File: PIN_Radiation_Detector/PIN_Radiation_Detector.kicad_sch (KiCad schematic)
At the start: 21 parts, among them J1 Conn_01x03, Q1 MMBF4392LT1G, U1 LM358DR

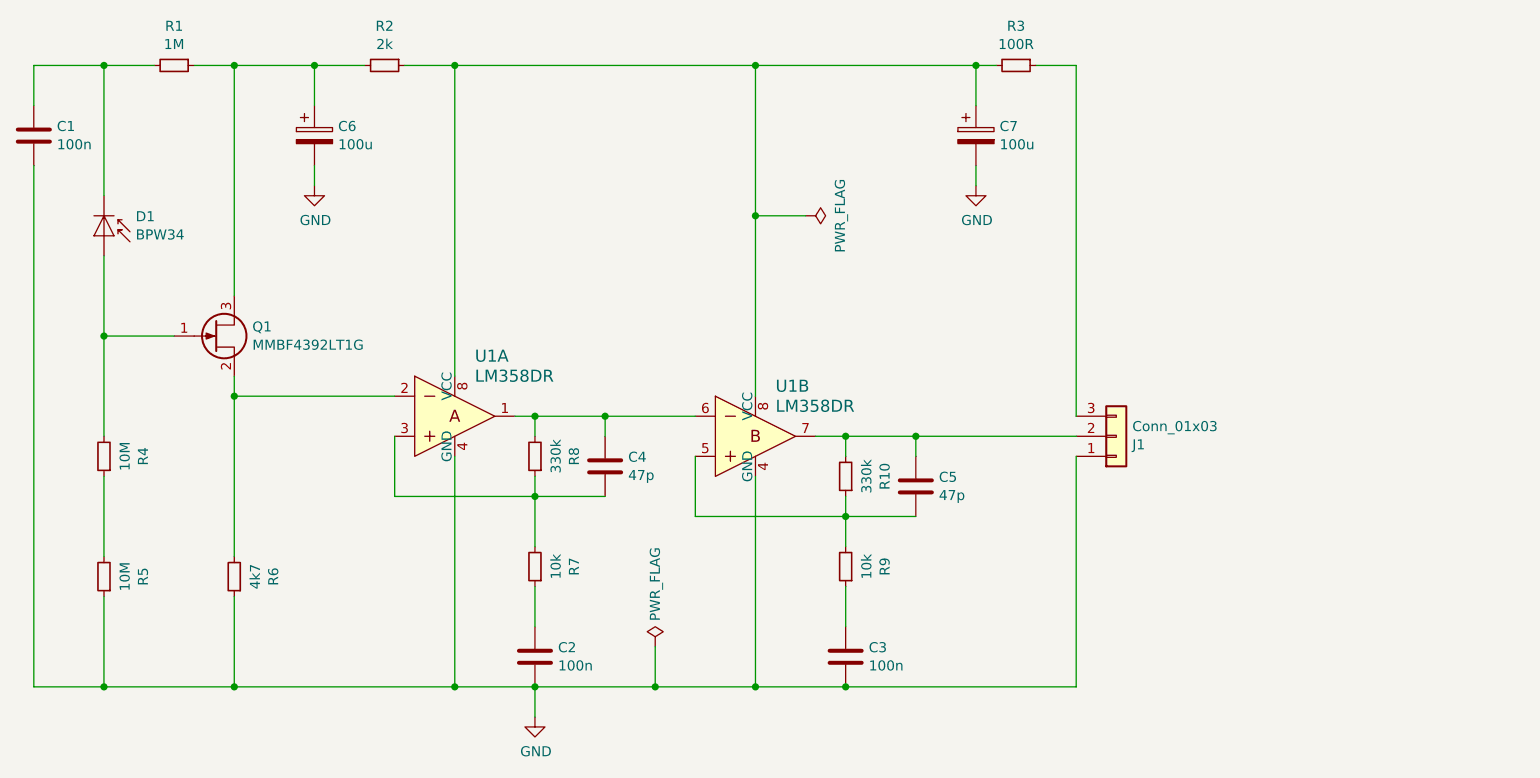
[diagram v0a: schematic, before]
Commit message: Add PDF schematic plot and minor text notes
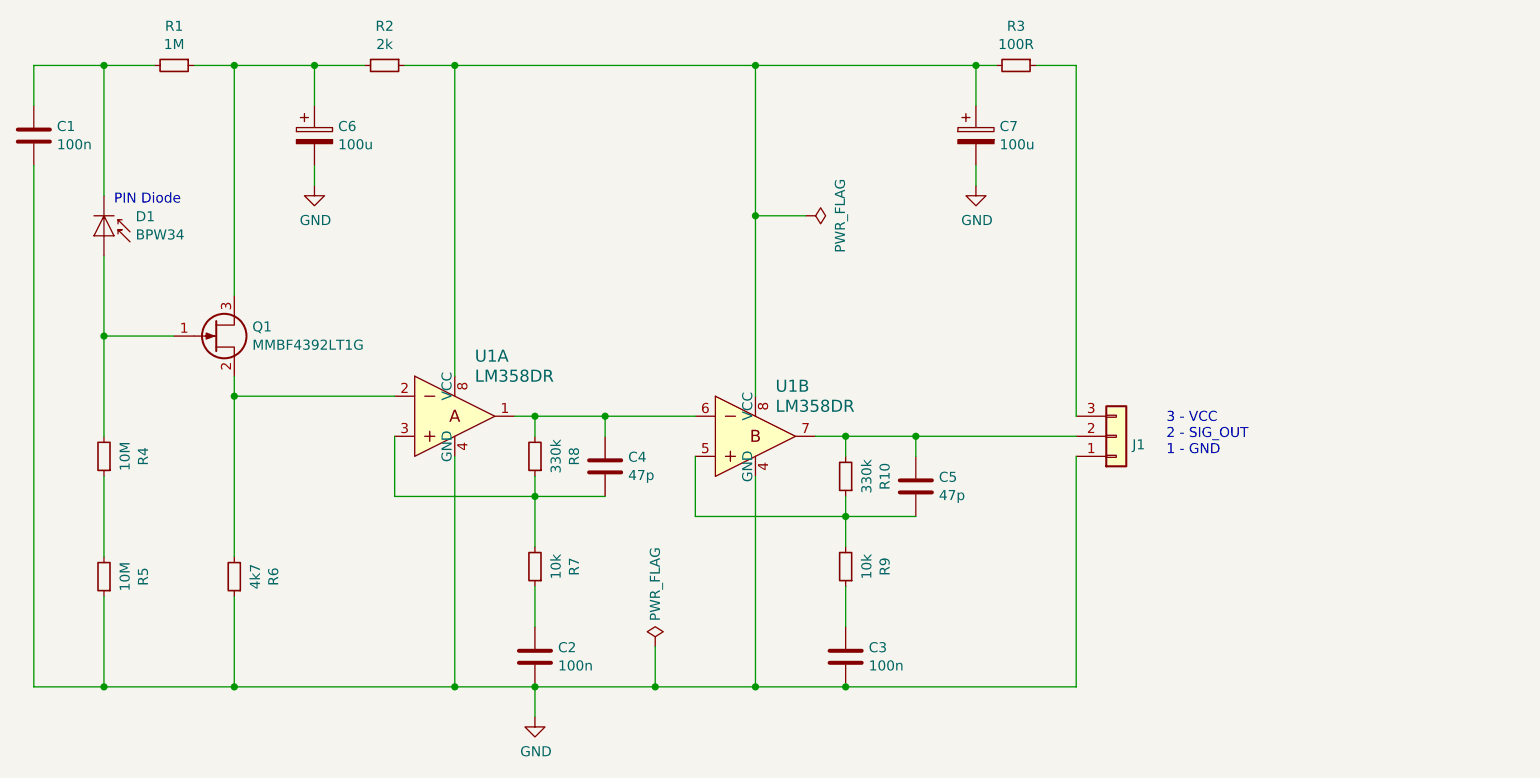
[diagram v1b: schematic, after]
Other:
- note added: "3 - VCC 2 - SIG_OUT 1 - GND"
- note added: "PIN Diode"
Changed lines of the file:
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@@
 (kicad_sch (version 20230121) (generator eeschema)
-  (paper "A4")
+  (paper "USLetter")
   (title_block
     (title "PIN Diode Radiation Detector Breakout")
@@
     (stroke (width 0) (type default))
   )
+  (text "3 - VCC\n2 - SIG_OUT\n1 - GND" (at 219.71 92.71 0)
+    (effects (font (size 1.27 1.27)) (justify left bottom))
+  )
+  (text "PIN Diode" (at 86.36 60.96 0)
+    (effects (font (size 1.27 1.27)) (justify left bottom))
+  )
   (symbol (lib_id "Sensor_Optical:BPW34") (at 85.09 64.77 270) (unit 1)
     (in_bom yes) (on_board yes) (dnp no)
@@
     )
     (property "Value" "Conn_01x03" (at 215.392 88.9254 0)
-      (effects (font (size 1.27 1.27)) (justify left))
+      (effects (font (size 1.27 1.27)) (justify left) hide)
     )
     (property "Footprint" "Pin_Headers:Pin_Header_Straight_1x03_Pitch2.54mm" (at 213.36 90.17 0)

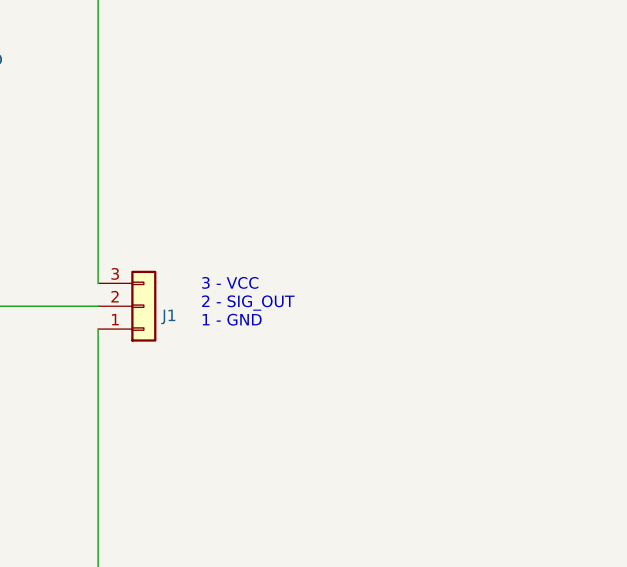
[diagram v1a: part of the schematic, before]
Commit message: Add VCC=5V recommended note
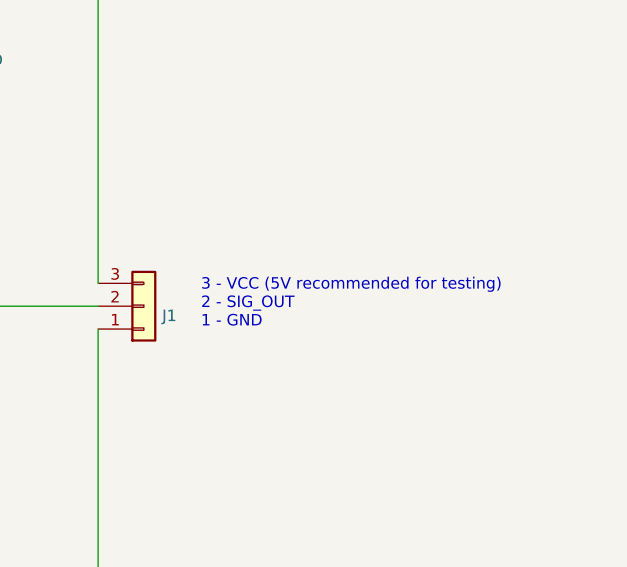
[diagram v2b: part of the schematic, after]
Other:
- note added: "3 - VCC (5V recommended for testing) 2 - SIG_OUT 1 - GND"
- note removed: "3 - VCC 2 - SIG_OUT 1 - GND"
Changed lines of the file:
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@@
     (stroke (width 0) (type default))
   )
-  (text "3 - VCC\n2 - SIG_OUT\n1 - GND" (at 219.71 92.71 0)
+  (text "3 - VCC (5V recommended for testing)\n2 - SIG_OUT\n1 - GND"
+    (at 219.71 92.71 0)
     (effects (font (size 1.27 1.27)) (justify left bottom))
   )

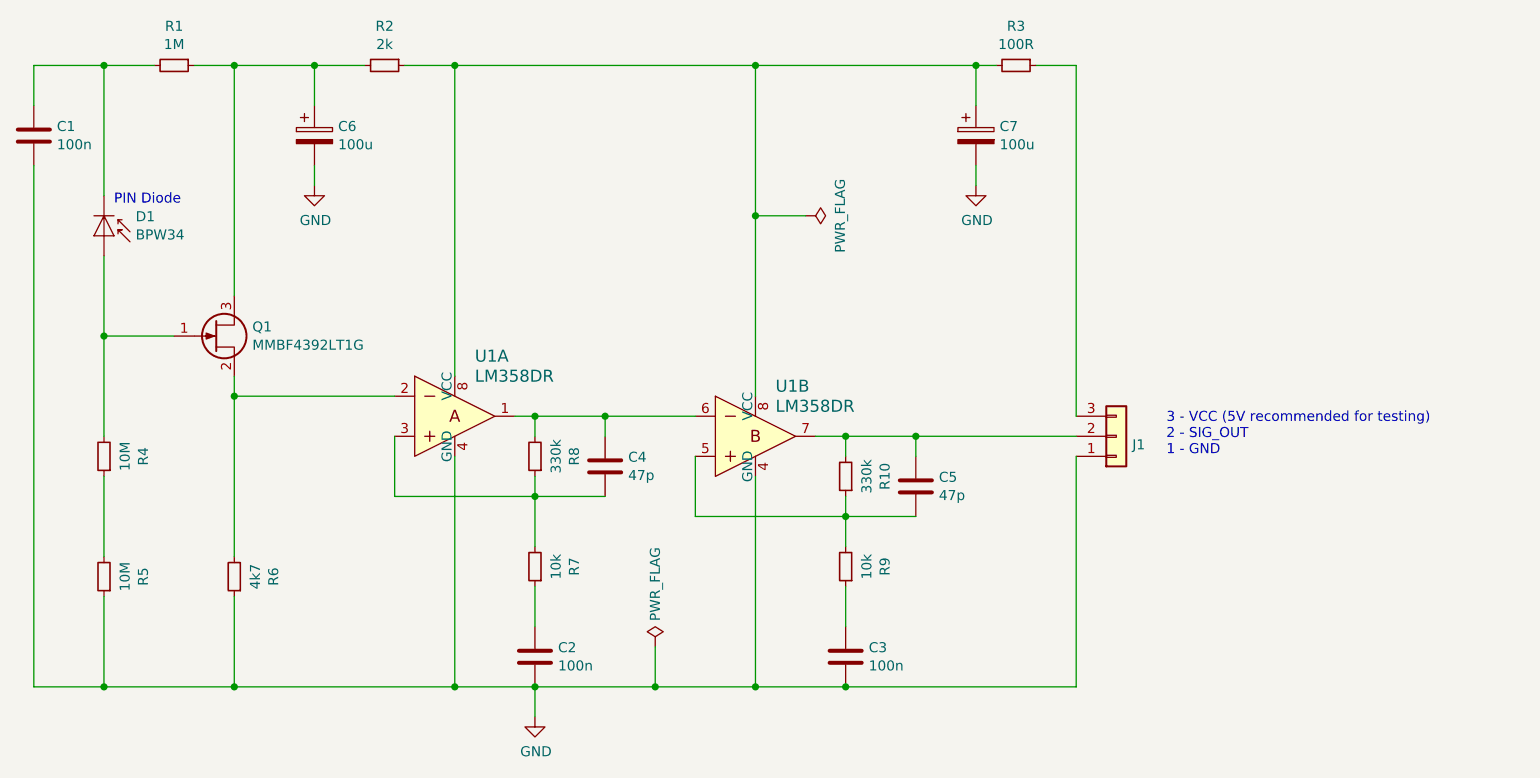
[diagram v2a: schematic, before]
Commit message: fix stupid op-amp input terminal swap error
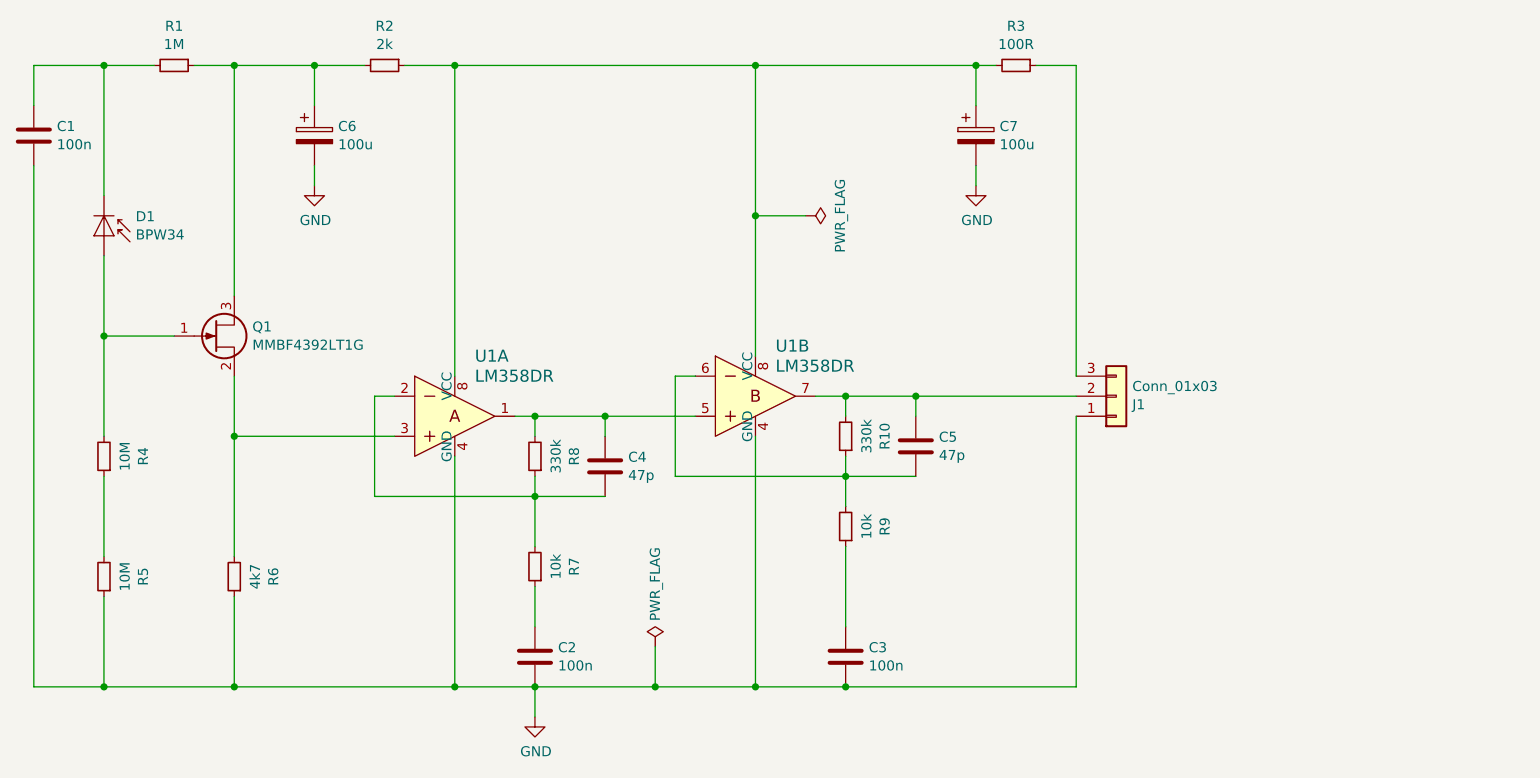
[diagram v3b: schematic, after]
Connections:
- net at C4.1, R8.2, U1.1: now also U1.5; no longer U1.6
- net at C4.2, R7.2, R8.1: now also U1.2; no longer U1.3
- net at Q1.2 (S), R6.2: now also U1.3; no longer U1.2
- net at C5.2, R10.1, R9.2: now also U1.6; no longer U1.5
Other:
- note removed: "3 - VCC (5V recommended for testing) 2 - SIG_OUT 1 - GND"
- note removed: "PIN Diode"
- moved on the sheet: C5, J1, R10, R9, U1B
